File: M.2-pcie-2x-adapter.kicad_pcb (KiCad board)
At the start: 4 copper layers, 100 x 95.5 mm, 34 parts, among them J1 Connector_PCIe_x4, U1 SY8204, U2 M.2-NGFF-Full

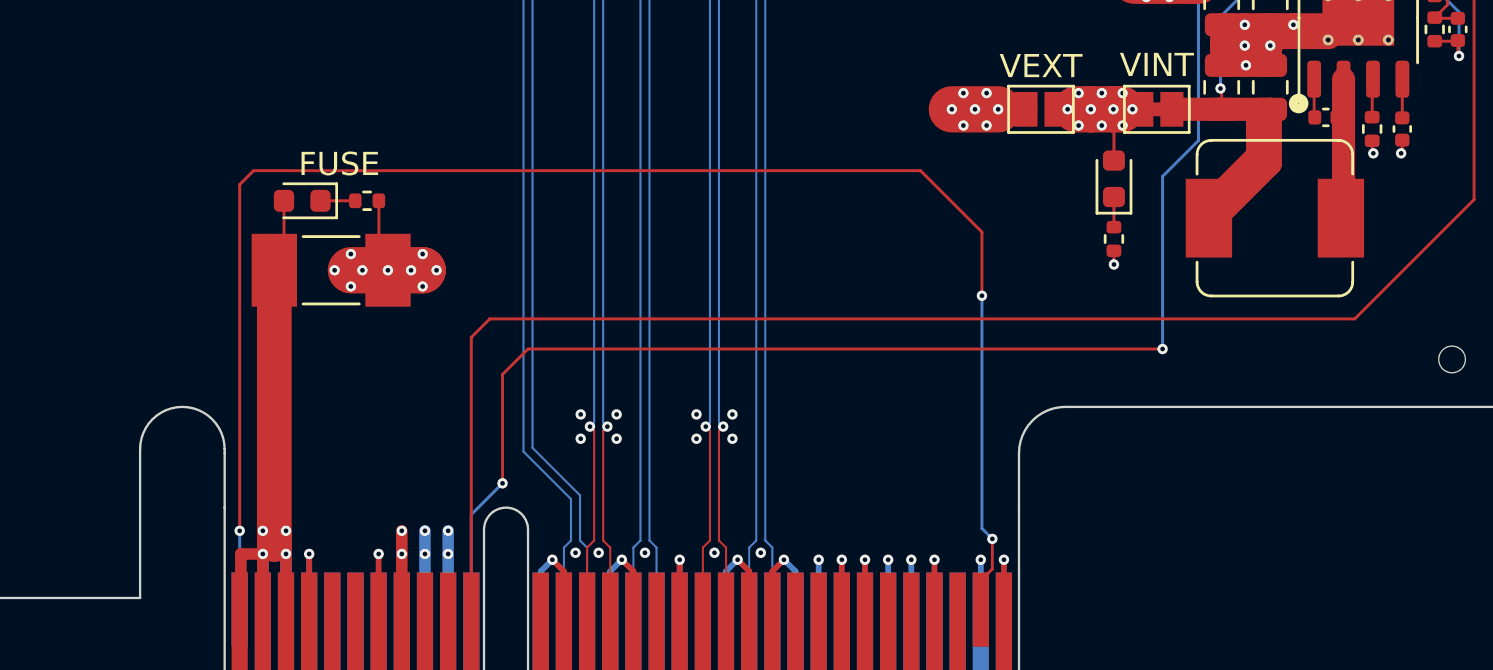
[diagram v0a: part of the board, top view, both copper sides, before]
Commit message: Upgraded files to kicad 9.0
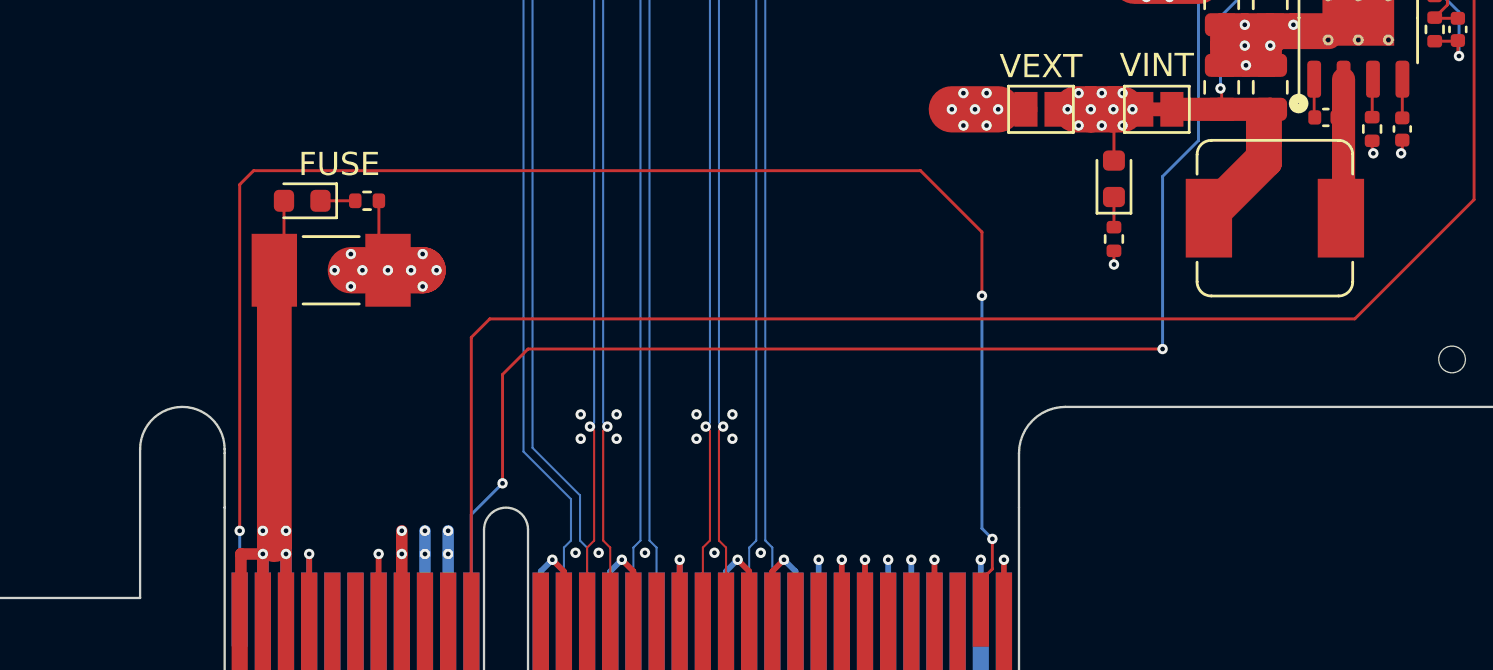
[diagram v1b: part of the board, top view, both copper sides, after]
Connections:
- net /~CLKREQ renamed /~{CLKREQ}
- net /~PERST renamed /~{PERST}
- net /~WAKE renamed /~{WAKE}
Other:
- net class Default removed
